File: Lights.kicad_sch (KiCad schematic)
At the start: 18 parts, among them Q2 NMOS, Q5 NMOS

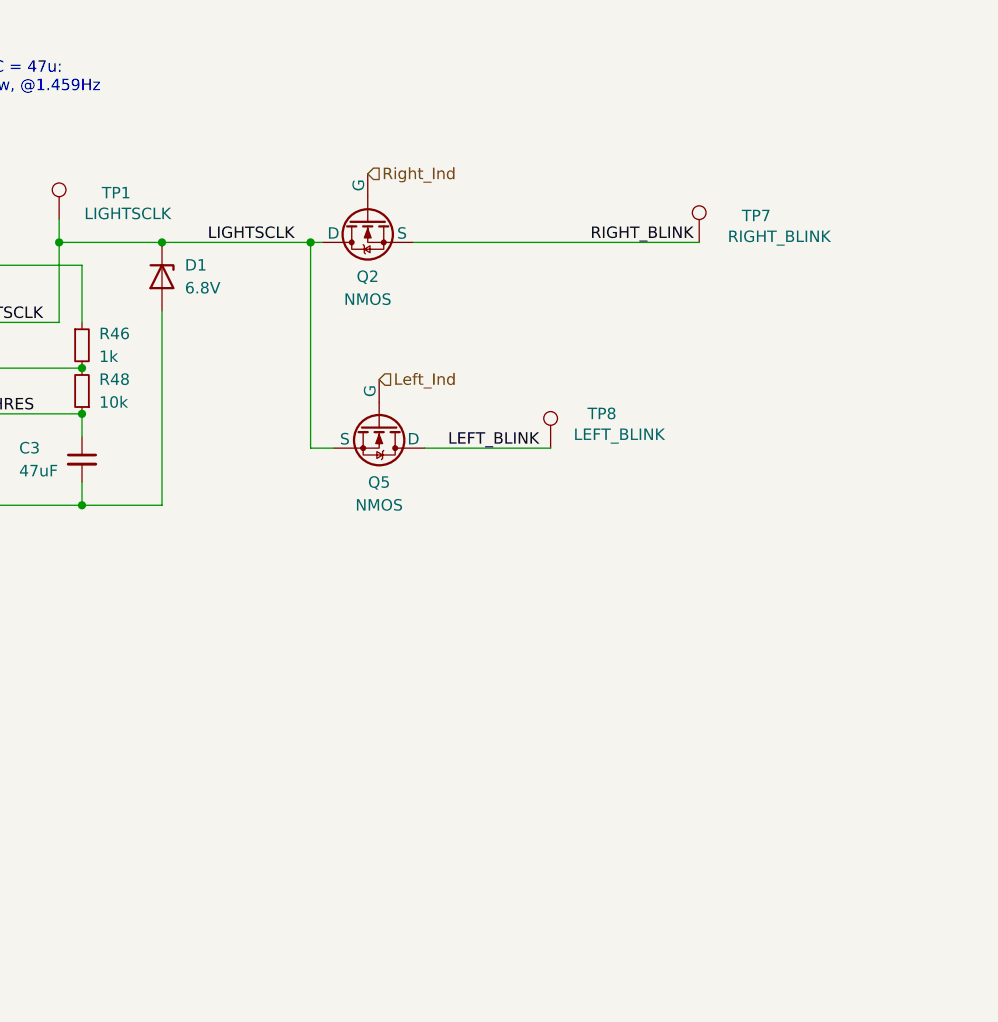
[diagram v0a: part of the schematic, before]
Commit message: Flipped optoisolators, changed resistor values, added second connector to motor can and disconnected shield pins for now since I haven't seen them used (will chack against old version to see what the circuit looked like), copied power-in circuit from contactor board, added optoisolator to timer and blinker light connection.
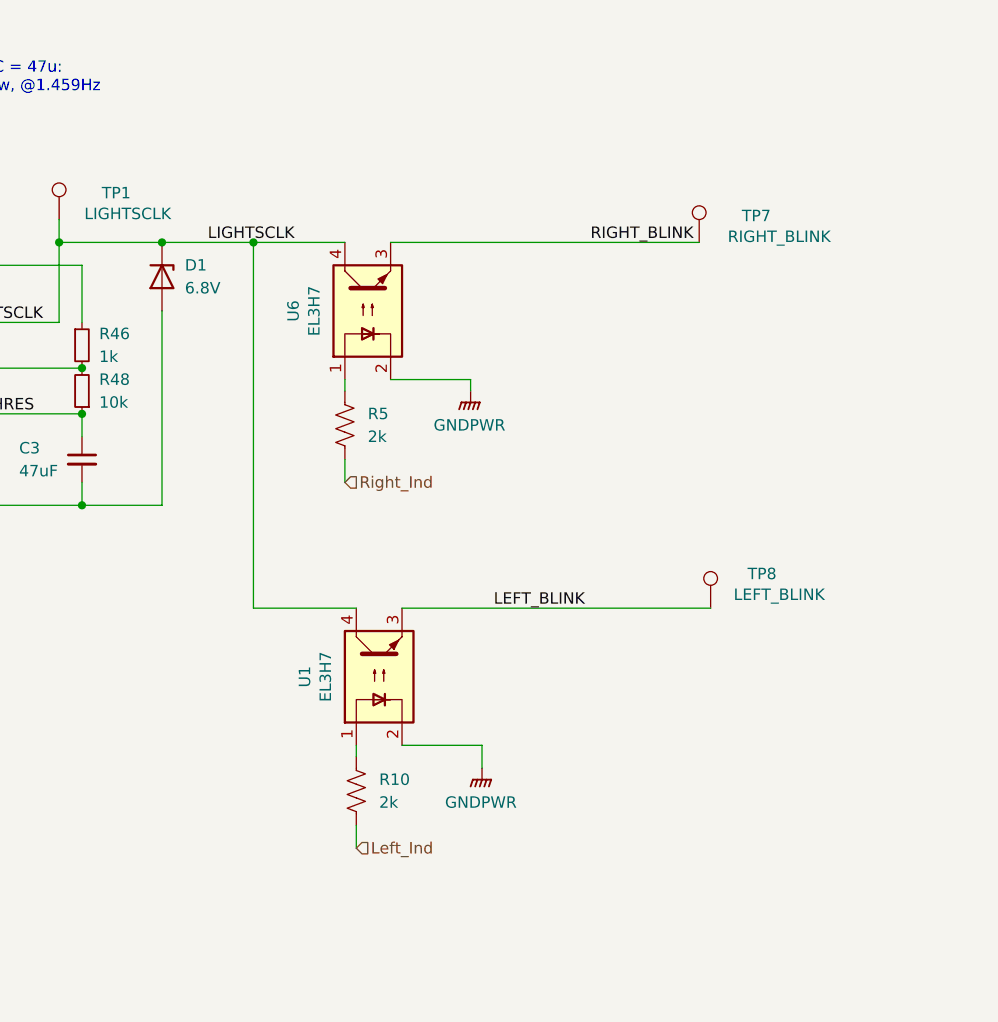
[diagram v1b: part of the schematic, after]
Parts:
- removed Q2, Q5: NMOS, symbol Simulation_SPICE:NMOS
- added R10, R5: 2k, symbol Device:R_US
- added U1, U6: EL3H7, Package_DIP:DIP-4_W7.62mm, symbol Isolator:SFH617A-1
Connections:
- net LEFT_BLINK: now also U1.3
- net LIGHTSCLK: now also U1.4, U6.4
- net Left_Ind: now also R10.2
- net RIGHT_BLINK: now also U6.3
- net Right_Ind: now also R5.2
- new net: R5.1, U6.1
- new net: R10.1, U1.1
- new net GNDPWR: U1.2, U6.2
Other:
- moved on the sheet: TP8

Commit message: Added footprints. I think this is everything except the fuse.
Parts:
- R10, R5: footprint (none) -> Resistor_SMD:R_0805_2012Metric
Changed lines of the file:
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@@
 			)
 		)
-		(property "Footprint" ""
+		(property "Footprint" "Resistor_SMD:R_0805_2012Metric"
 			(at 168.656 98.044 90)
 			(effects
@@
 			)
 		)
-		(property "Footprint" ""
+		(property "Footprint" "Resistor_SMD:R_0805_2012Metric"
 			(at 169.926 138.684 90)
 			(effects

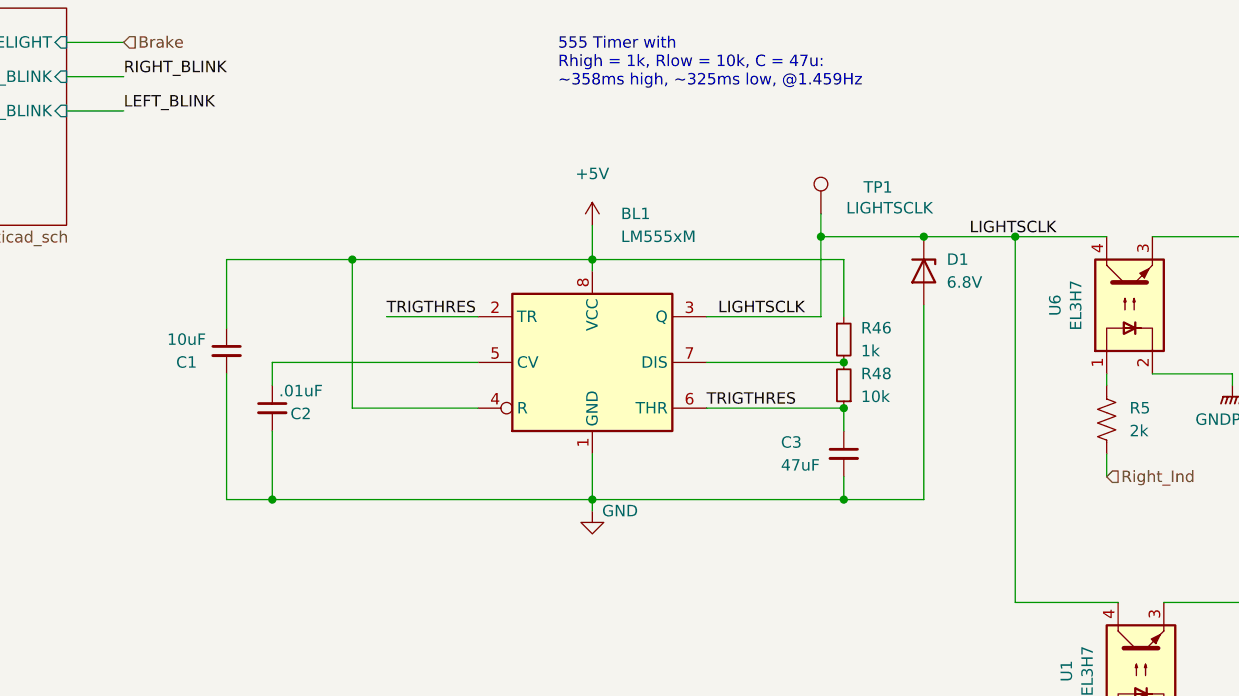
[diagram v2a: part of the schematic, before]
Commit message: Fuse footprint added and blinker changed to software
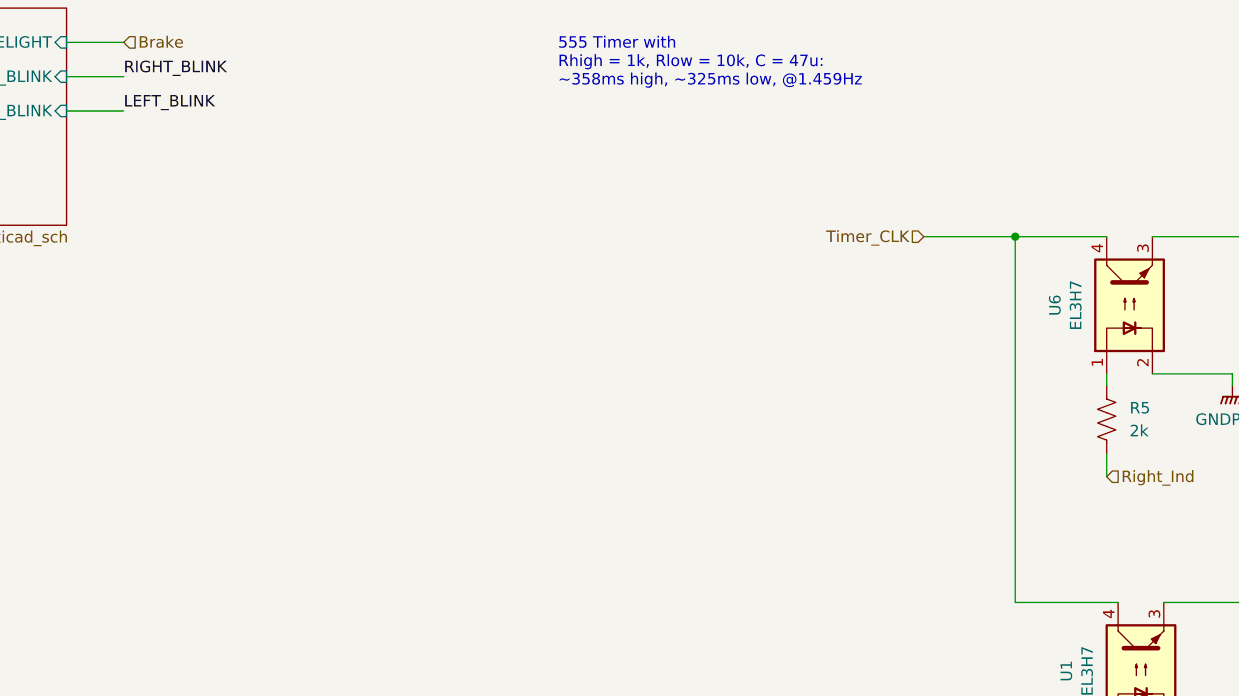
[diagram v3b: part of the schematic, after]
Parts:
- removed BL1: LM555xM, Package_SO:SOIC-8_3.9x4.9mm_P1.27mm, symbol Timer:LM555xM
- removed C1: 10uF, Capacitor_SMD:C_0805_2012Metric, symbol Device:C_Small
- removed C2: .01uF, Capacitor_SMD:C_0805_2012Metric, symbol Device:C_Small
- removed C3: 47uF, Capacitor_SMD:C_0805_2012Metric, symbol Device:C_Small
- removed D1: 6.8V, Diode_SMD:D_0805_2012Metric, symbol Device:D_Zener
- removed R46: 1k, Resistor_SMD:R_0805_2012Metric, symbol Device:R_Small
- removed R48: 10k, Resistor_SMD:R_0805_2012Metric, symbol Device:R_Small
- removed TP1: LIGHTSCLK, TestPoint:TestPoint_Pad_1.5x1.5mm, symbol Connector:TestPoint
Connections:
- net LIGHTSCLK renamed Timer_CLK

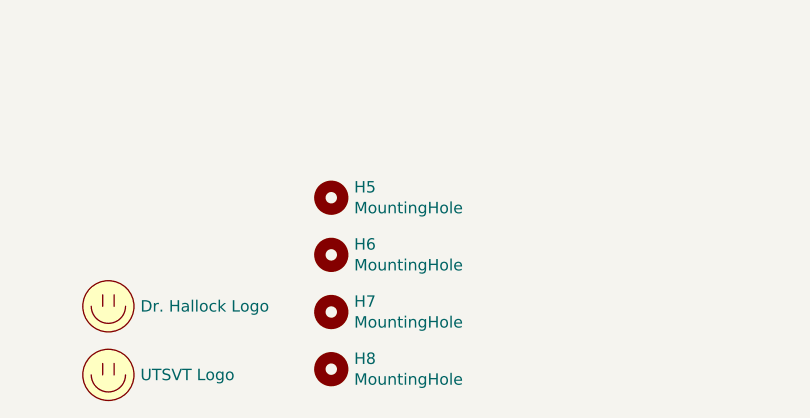
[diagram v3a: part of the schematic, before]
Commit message: Started cleaning some comments, changed EL3H7 data sheet link, removed extra motor CAN connector and changed original one to match (I think) motor controller connector, removed extra mounting holes, removed hierarchical power labels.
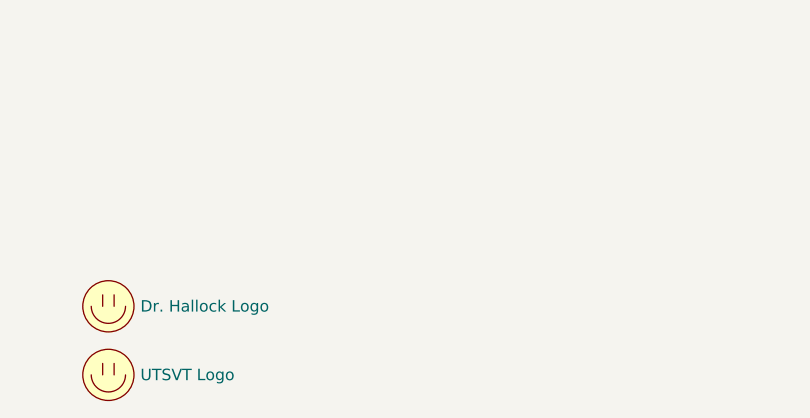
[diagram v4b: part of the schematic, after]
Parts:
- removed H5, H6, H7, H8: MountingHole, MountingHole:MountingHole_3mm, symbol Mechanical:MountingHole
